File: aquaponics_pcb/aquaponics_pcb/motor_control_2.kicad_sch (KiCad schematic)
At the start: 8 parts, among them IC5 DRV8214RTER, J6 Screw_Terminal_01x02

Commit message: add initial pcb layout
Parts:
- IC5: footprint QFN50P300X300X80-17N-D -> SamacSys_Parts:QFN50P300X300X80-17N-D
- J6: footprint (none) -> Connector_Phoenix_GMSTB:PhoenixContact_GMSTBA_2,5_2-G_1x02_P7.50mm_Horizontal
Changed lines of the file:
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@@
 			)
 		)
-		(property "Footprint" ""
+		(property "Footprint" "Connector_Phoenix_GMSTB:PhoenixContact_GMSTBA_2,5_2-G_1x02_P7.50mm_Horizontal"
 			(at 140.97 130.81 0)
 			(effects
@@
 			)
 		)
-		(property "Footprint" "QFN50P300X300X80-17N-D"
+		(property "Footprint" "SamacSys_Parts:QFN50P300X300X80-17N-D"
 			(at 153.67 171.12 0)
 			(effects

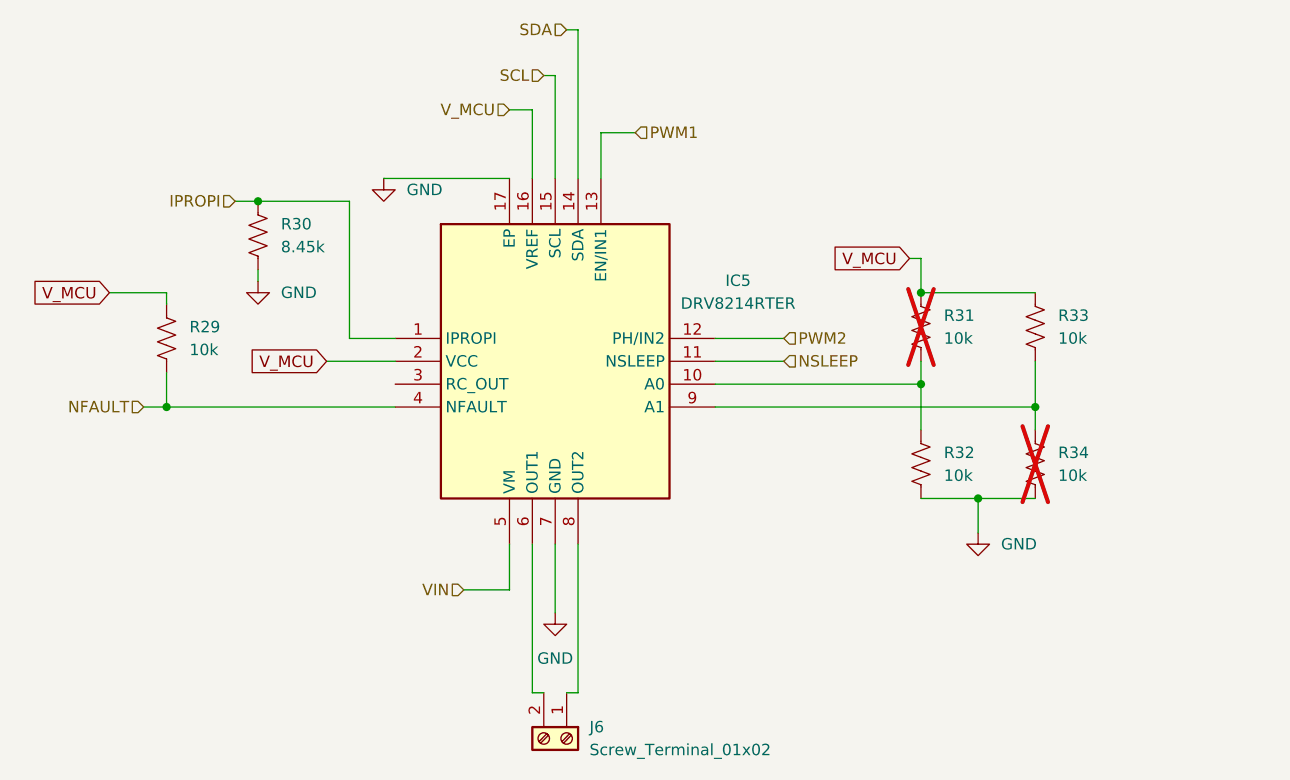
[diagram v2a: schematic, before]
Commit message: finish ground and power pours. fix rules and run final DRC. export gerbers
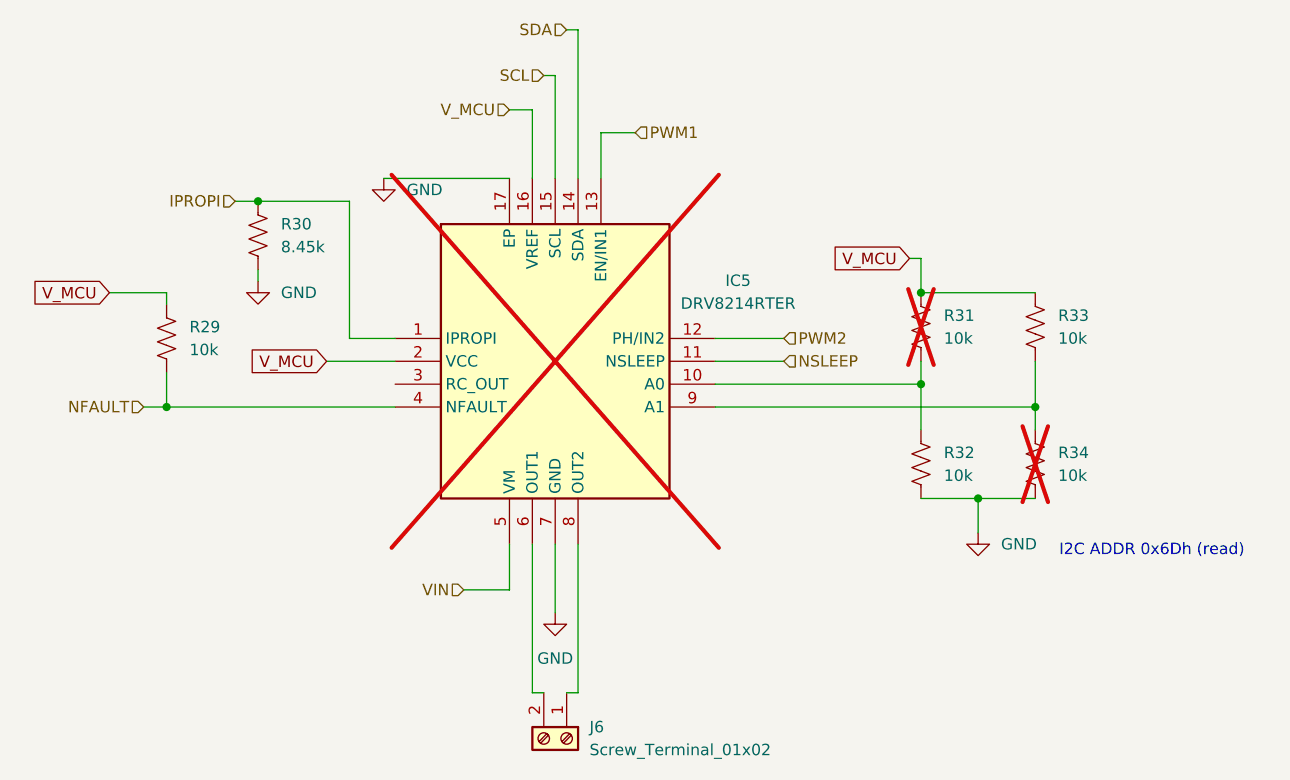
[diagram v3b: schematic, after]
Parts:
- IC5: now not fitted
- R29, R32, R33: JLCPCB Part # (none) -> C98220; LCSC Part Number (none) -> C98220
- R30: JLCPCB Part # (none) -> C2933263; LCSC Part Number (none) -> C2933263
- R31, R34: LCSC Part Number (none) -> C98220
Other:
- note added: "I2C ADDR 0x6Dh (read)"
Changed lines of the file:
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@@
 	(generator_version "9.0")
 	(paper "A4")
+	(text "I2C ADDR 0x6Dh (read)"
+		(exclude_from_sim no)
+		(at 205.994 109.982 0)
+		(effects
+			(font
+				(size 1.27 1.27)
+			)
+		)
+	)
 	(junction
 		(at 180.34 81.28)
@@
 			)
 		)
+		(property "LCSC Part Number" "C98220"
+			(at 193.04 100.33 0)
+			(effects
+				(font
+					(size 1.27 1.27)
+				)
+				(hide yes)
+			)
+		)
+		(property "JLCPCB Part #" ""
+			(at 193.04 100.33 0)
+			(effects
+				(font
+					(size 1.27 1.27)
+				)
+				(hide yes)
+			)
+		)
 		(pin "1"
 		)
@@
 			)
 		)
+		(property "LCSC Part Number" "C98220"
+			(at 96.52 86.36 0)
+			(effects
+				(font
+					(size 1.27 1.27)
+				)
+				(hide yes)
+			)
+		)
+		(property "JLCPCB Part #" "C98220"
+			(at 96.52 86.36 0)
+			(effects
+				(font
+					(size 1.27 1.27)
+				)
+				(hide yes)
+			)
+		)
 		(pin "1"
 		)
@@
 			)
 		)
+		(property "LCSC Part Number" "C98220"
+			(at 180.34 100.33 0)
+			(effects
+				(font
+					(size 1.27 1.27)
+				)
+				(hide yes)
+			)
+		)
+		(property "JLCPCB Part #" "C98220"
+			(at 180.34 100.33 0)
+			(effects
+				(font
+					(size 1.27 1.27)
+				)
+				(hide yes)
+			)
+		)
 		(pin "1"
 		)
@@
 			)
 		)
+		(property "LCSC Part Number" ""
+			(at 140.97 130.81 90)
+			(effects
+				(font
+					(size 1.27 1.27)
+				)
+				(hide yes)
+			)
+		)
+		(property "JLCPCB Part #" ""
+			(at 140.97 130.81 90)
+			(effects
+				(font
+					(size 1.27 1.27)
+				)
+				(hide yes)
+			)
+		)
 		(pin "2"
 		)
@@
 			)
 		)
+		(property "LCSC Part Number" "C98220"
+			(at 193.04 85.09 0)
+			(effects
+				(font
+					(size 1.27 1.27)
+				)
+				(hide yes)
+			)
+		)
+		(property "JLCPCB Part #" "C98220"
+			(at 193.04 85.09 0)
+			(effects
+				(font
+					(size 1.27 1.27)
+				)
+				(hide yes)
+			)
+		)
 		(pin "1"
 		)
@@
 		(in_bom yes)
 		(on_board yes)
-		(dnp no)
+		(dnp yes)
 		(fields_autoplaced yes)
 		(property "Reference" "IC5"
@@
 				)
 				(justify left top)
+				(hide yes)
+			)
+		)
+		(property "LCSC Part Number" ""
+			(at 121.92 86.36 0)
+			(effects
+				(font
+					(size 1.27 1.27)
+				)
+				(hide yes)
+			)
+		)
+		(property "JLCPCB Part #" ""
+			(at 121.92 86.36 0)
+			(effects
+				(font
+					(size 1.27 1.27)
+				)
 				(hide yes)
 			)
@@
 			)
 		)
+		(property "LCSC Part Number" "C98220"
+			(at 180.34 85.09 0)
+			(effects
+				(font
+					(size 1.27 1.27)
+				)
+				(hide yes)
+			)
+		)
+		(property "JLCPCB Part #" ""
+			(at 180.34 85.09 0)
+			(effects
+				(font
+					(size 1.27 1.27)
+				)
+				(hide yes)
+			)
+		)
 		(pin "1"
 		)
@@
 			(at 106.68 74.93 0)
 			(effects
+				(font
+					(size 1.27 1.27)
+				)
+				(hide yes)
+			)
+		)
+		(property "LCSC Part Number" "C2933263"
+			(at 106.68 74.93 0)
+			(effects
+				(font
+					(size 1.27 1.27)
+				)
+				(hide yes)
+			)
+		)
+		(property "JLCPCB Part #" "C2933263"
+			(at 106.68 74.93 0)
+			(effects
